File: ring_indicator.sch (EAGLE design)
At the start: 21 parts, among them Q2 BUZ11

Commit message: v0.2-produced
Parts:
- FRITZBOX, INPUT_12V, LICHT1, LICHT2, RUNDUMLEUCHTE: value (none) -> CON_23.81; device pinhead:PINHD-1X2 -> pcaroli:CON_23.81
- R1, R2, R3, R4: device rcl:R-EU_0204/5 -> rcl:R-EU_0207/10
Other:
- moved on the sheet: FRITZBOX, INPUT_12V, LICHT1, LICHT2, RUNDUMLEUCHTE
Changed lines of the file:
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@@
 <layer number="51" name="tDocu" color="6" fill="1" visible="no" active="no"/>
 <layer number="52" name="bDocu" color="7" fill="1" visible="no" active="no"/>
+<layer number="90" name="Modules" color="5" fill="1" visible="yes" active="yes"/>
 <layer number="91" name="Nets" color="2" fill="1" visible="yes" active="yes"/>
 <layer number="92" name="Busses" color="1" fill="1" visible="yes" active="yes"/>
@@
 <parts>
 <part name="PHONE_IN" library="con-wenzhou-yihua" deviceset="YH-55-10" device=""/>
-<part name="FRITZBOX" library="pinhead" deviceset="PINHD-1X2" device=""/>
-<part name="LICHT1" library="pinhead" deviceset="PINHD-1X2" device=""/>
-<part name="LICHT2" library="pinhead" deviceset="PINHD-1X2" device=""/>
-<part name="RUNDUMLEUCHTE" library="pinhead" deviceset="PINHD-1X2" device=""/>
+<part name="FRITZBOX" library="pcaroli" deviceset="CON_2" device="3.81"/>
+<part name="LICHT1" library="pcaroli" deviceset="CON_2" device="3.81"/>
+<part name="LICHT2" library="pcaroli" deviceset="CON_2" device="3.81"/>
+<part name="RUNDUMLEUCHTE" library="pcaroli" deviceset="CON_2" device="3.81"/>
 <part name="SUPPLY1" library="supply2" deviceset="GND" device=""/>
 <part name="P+1" library="supply1" deviceset="VCC" device=""/>
@@
 <part name="SUPPLY2" library="supply2" deviceset="GND" device=""/>
 <part name="SUPPLY3" library="supply2" deviceset="GND" device=""/>
-<part name="INPUT_12V" library="pinhead" deviceset="PINHD-1X2" device=""/>
+<part name="INPUT_12V" library="pcaroli" deviceset="CON_2" device="3.81"/>
 <part name="SUPPLY4" library="supply2" deviceset="GND" device=""/>
 <part name="P+4" library="supply1" deviceset="VCC" device=""/>
 <part name="C1" library="resistor" deviceset="C-EU" device="102-064X133" value="470n"/>
 <part name="C2" library="rcl" deviceset="CPOL-EU" device="E3.5-8" value="47u"/>
-<part name="R1" library="rcl" deviceset="R-EU_" device="0204/5" value="1M"/>
-<part name="R2" library="rcl" deviceset="R-EU_" device="0204/5" value="1k"/>
+<part name="R1" library="rcl" deviceset="R-EU_" device="0207/10" value="1M"/>
+<part name="R2" library="rcl" deviceset="R-EU_" device="0207/10" value="1k"/>
 <part name="D1" library="diode" deviceset="1N4004" device=""/>
 <part name="D2" library="diode" deviceset="1N4004" device=""/>
 <part name="D3" library="diode" deviceset="1N4004" device=""/>
 <part name="D4" library="diode" deviceset="1N4004" device=""/>
-<part name="R3" library="rcl" deviceset="R-EU_" device="0204/5" value="2k2"/>
+<part name="R3" library="rcl" deviceset="R-EU_" device="0207/10" value="2k2"/>
 <part name="LED1" library="led" deviceset="LED" device="5MM"/>
-<part name="R4" library="rcl" deviceset="R-EU_" device="0204/5" value="100k"/>
+<part name="R4" library="rcl" deviceset="R-EU_" device="0207/10" value="100k"/>
 <part name="OK1" library="optocoupler" deviceset="4N*?M" device="" technology="27"/>
 <part name="Q2" library="transistor-fet" deviceset="BUZ11" device=""/>
@@
 <instance part="LICHT1" gate="G$1" x="256.54" y="88.9" rot="MR180"/>
 <instance part="LICHT2" gate="G$1" x="256.54" y="60.96" rot="MR180"/>
-<instance part="RUNDUMLEUCHTE" gate="G$1" x="220.98" y="35.56" rot="MR180"/>
+<instance part="RUNDUMLEUCHTE" gate="G$1" x="220.98" y="33.02" rot="MR180"/>
 <instance part="SUPPLY1" gate="GND" x="246.38" y="109.22" rot="MR0"/>
 <instance part="P+1" gate="VCC" x="246.38" y="121.92" rot="MR0"/>
@@
 <segment>
 <pinref part="FRITZBOX" gate="G$1" pin="1"/>
-<wire x1="254" y1="114.3" x2="246.38" y2="114.3" width="0.1524" layer="91"/>
 <wire x1="246.38" y1="114.3" x2="246.38" y2="111.76" width="0.1524" layer="91"/>
 <pinref part="SUPPLY1" gate="GND" pin="GND"/>
@@
 <segment>
 <pinref part="LICHT1" gate="G$1" pin="1"/>
-<wire x1="254" y1="86.36" x2="246.38" y2="86.36" width="0.1524" layer="91"/>
 <wire x1="246.38" y1="86.36" x2="246.38" y2="83.82" width="0.1524" layer="91"/>
 <pinref part="SUPPLY2" gate="GND" pin="GND"/>
@@
 <segment>
 <pinref part="LICHT2" gate="G$1" pin="1"/>
-<wire x1="254" y1="58.42" x2="246.38" y2="58.42" width="0.1524" layer="91"/>
 <wire x1="246.38" y1="58.42" x2="246.38" y2="55.88" width="0.1524" layer="91"/>
 <pinref part="SUPPLY3" gate="GND" pin="GND"/>
@@
 <wire x1="68.58" y1="111.76" x2="68.58" y2="109.22" width="0.1524" layer="91"/>
 <pinref part="INPUT_12V" gate="G$1" pin="1"/>
-<wire x1="35.56" y1="116.84" x2="40.64" y2="116.84" width="0.1524" layer="91"/>
+<wire x1="43.18" y1="116.84" x2="40.64" y2="116.84" width="0.1524" layer="91"/>
 <wire x1="40.64" y1="116.84" x2="40.64" y2="111.76" width="0.1524" layer="91"/>
 <wire x1="40.64" y1="111.76" x2="50.8" y2="111.76" width="0.1524" layer="91"/>
@@
 <segment>
 <pinref part="FRITZBOX" gate="G$1" pin="2"/>
-<wire x1="254" y1="116.84" x2="246.38" y2="116.84" width="0.1524" layer="91"/>
 <wire x1="246.38" y1="116.84" x2="246.38" y2="119.38" width="0.1524" layer="91"/>
 <pinref part="P+1" gate="VCC" pin="VCC"/>
@@
 <segment>
 <pinref part="LICHT1" gate="G$1" pin="2"/>
-<wire x1="254" y1="88.9" x2="246.38" y2="88.9" width="0.1524" layer="91"/>
 <wire x1="246.38" y1="88.9" x2="246.38" y2="91.44" width="0.1524" layer="91"/>
 <pinref part="P+2" gate="VCC" pin="VCC"/>
@@
 <segment>
 <pinref part="LICHT2" gate="G$1" pin="2"/>
-<wire x1="254" y1="60.96" x2="246.38" y2="60.96" width="0.1524" layer="91"/>
 <wire x1="246.38" y1="60.96" x2="246.38" y2="63.5" width="0.1524" layer="91"/>
 <pinref part="P+3" gate="VCC" pin="VCC"/>
@@
 <pinref part="RUNDUMLEUCHTE" gate="G$1" pin="2"/>
 <pinref part="OK1" gate="G$1" pin="COL"/>
-<wire x1="187.96" y1="35.56" x2="218.44" y2="35.56" width="0.1524" layer="91"/>
+<wire x1="187.96" y1="35.56" x2="210.82" y2="35.56" width="0.1524" layer="91"/>
 <wire x1="182.88" y1="0" x2="187.96" y2="0" width="0.1524" layer="91"/>
 <wire x1="187.96" y1="0" x2="187.96" y2="35.56" width="0.1524" layer="91"/>
@@
 <wire x1="68.58" y1="124.46" x2="68.58" y2="127" width="0.1524" layer="91"/>
 <pinref part="INPUT_12V" gate="G$1" pin="2"/>
-<wire x1="35.56" y1="119.38" x2="40.64" y2="119.38" width="0.1524" layer="91"/>
+<wire x1="43.18" y1="121.92" x2="40.64" y2="119.38" width="0.1524" layer="91"/>
 <wire x1="40.64" y1="119.38" x2="40.64" y2="124.46" width="0.1524" layer="91"/>
 <wire x1="40.64" y1="124.46" x2="50.8" y2="124.46" width="0.1524" layer="91"/>
@@
 <segment>
 <pinref part="RUNDUMLEUCHTE" gate="G$1" pin="1"/>
-<wire x1="218.44" y1="33.02" x2="208.28" y2="33.02" width="0.1524" layer="91"/>
+<wire x1="210.82" y1="30.48" x2="208.28" y2="30.48" width="0.1524" layer="91"/>
 <pinref part="Q2" gate="G$1" pin="D"/>
-<wire x1="208.28" y1="0" x2="208.28" y2="33.02" width="0.1524" layer="91"/>
-</segment>
-</net>
+<wire x1="208.28" y1="0" x2="208.28" y2="30.48" width="0.1524" layer="91"/>
+</segment>
+</net>

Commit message: v0.2.1-cleanup
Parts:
- removed C3: (no value), capacitor-wima:C2,5-3
- removed C5: (no value), resistor:CPOL-EUTT2D6
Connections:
- net GND: no longer C3.2, C5.-
- net VCC: no longer C3.1, C5.+
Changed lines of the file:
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@@
 <part name="SUPPLY6" library="supply2" deviceset="GND" device=""/>
 <part name="SUPPLY7" library="supply2" deviceset="GND" device=""/>
-<part name="C3" library="capacitor-wima" deviceset="C" device="2,5-3"/>
-<part name="C5" library="resistor" deviceset="CPOL-EU" device="TT2D6"/>
 </parts>
 <sheets>
@@
 <instance part="SUPPLY3" gate="GND" x="246.38" y="53.34" rot="MR0"/>
 <instance part="INPUT_12V" gate="G$1" x="33.02" y="119.38" rot="R180"/>
-<instance part="SUPPLY4" gate="GND" x="68.58" y="106.68"/>
-<instance part="P+4" gate="VCC" x="68.58" y="129.54"/>
+<instance part="SUPPLY4" gate="GND" x="43.18" y="111.76"/>
+<instance part="P+4" gate="VCC" x="43.18" y="127"/>
 <instance part="C1" gate="G$1" x="93.98" y="15.24" rot="R270"/>
 <instance part="C2" gate="G$1" x="185.42" y="-17.78"/>
@@
 <instance part="SUPPLY6" gate="GND" x="185.42" y="-25.4"/>
 <instance part="SUPPLY7" gate="GND" x="210.82" y="-25.4"/>
-<instance part="C3" gate="G$1" x="50.8" y="119.38"/>
-<instance part="C5" gate="G$1" x="58.42" y="119.38"/>
 </instances>
 <busses>
@@
 </segment>
 <segment>
+<pinref part="INPUT_12V" gate="G$1" pin="1"/>
 <pinref part="SUPPLY4" gate="GND" pin="GND"/>
-<wire x1="68.58" y1="111.76" x2="68.58" y2="109.22" width="0.1524" layer="91"/>
-<pinref part="INPUT_12V" gate="G$1" pin="1"/>
-<wire x1="43.18" y1="116.84" x2="40.64" y2="116.84" width="0.1524" layer="91"/>
-<wire x1="40.64" y1="116.84" x2="40.64" y2="111.76" width="0.1524" layer="91"/>
-<wire x1="40.64" y1="111.76" x2="50.8" y2="111.76" width="0.1524" layer="91"/>
-<wire x1="50.8" y1="111.76" x2="58.42" y2="111.76" width="0.1524" layer="91"/>
-<wire x1="58.42" y1="111.76" x2="68.58" y2="111.76" width="0.1524" layer="91"/>
-<wire x1="58.42" y1="111.76" x2="58.42" y2="114.3" width="0.1524" layer="91"/>
-<junction x="58.42" y="111.76"/>
-<pinref part="C3" gate="G$1" pin="2"/>
-<wire x1="50.8" y1="111.76" x2="50.8" y2="114.3" width="0.1524" layer="91"/>
-<junction x="50.8" y="111.76"/>
-<pinref part="C5" gate="G$1" pin="-"/>
+<wire x1="43.18" y1="116.84" x2="43.18" y2="114.3" width="0.1524" layer="91"/>
 </segment>
 </net>
@@
 </segment>
 <segment>
+<pinref part="INPUT_12V" gate="G$1" pin="2"/>
+<wire x1="43.18" y1="121.92" x2="43.18" y2="124.46" width="0.1524" layer="91"/>
 <pinref part="P+4" gate="VCC" pin="VCC"/>
-<wire x1="68.58" y1="124.46" x2="68.58" y2="127" width="0.1524" layer="91"/>
-<pinref part="INPUT_12V" gate="G$1" pin="2"/>
-<wire x1="43.18" y1="121.92" x2="40.64" y2="119.38" width="0.1524" layer="91"/>
-<wire x1="40.64" y1="119.38" x2="40.64" y2="124.46" width="0.1524" layer="91"/>
-<wire x1="40.64" y1="124.46" x2="50.8" y2="124.46" width="0.1524" layer="91"/>
-<wire x1="50.8" y1="124.46" x2="58.42" y2="124.46" width="0.1524" layer="91"/>
-<wire x1="58.42" y1="124.46" x2="68.58" y2="124.46" width="0.1524" layer="91"/>
-<wire x1="58.42" y1="124.46" x2="58.42" y2="121.92" width="0.1524" layer="91"/>
-<junction x="58.42" y="124.46"/>
-<pinref part="C3" gate="G$1" pin="1"/>
-<wire x1="50.8" y1="124.46" x2="50.8" y2="121.92" width="0.1524" layer="91"/>
-<junction x="50.8" y="124.46"/>
-<pinref part="C5" gate="G$1" pin="+"/>
 </segment>
 </net>

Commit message: v0.2.2-layout simplified
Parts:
- R4: value 100k -> 50k
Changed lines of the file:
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@@
 <part name="R3" library="rcl" deviceset="R-EU_" device="0207/10" value="2k2"/>
 <part name="LED1" library="led" deviceset="LED" device="5MM"/>
-<part name="R4" library="rcl" deviceset="R-EU_" device="0207/10" value="100k"/>
+<part name="R4" library="rcl" deviceset="R-EU_" device="0207/10" value="50k"/>
 <part name="OK1" library="optocoupler" deviceset="4N*?M" device="" technology="27"/>
 <part name="Q2" library="transistor-fet" deviceset="BUZ11" device=""/>
@@
 <instance part="RUNDUMLEUCHTE" gate="G$1" x="220.98" y="33.02" rot="MR180"/>
 <instance part="SUPPLY1" gate="GND" x="246.38" y="109.22" rot="MR0"/>
-<instance part="P+1" gate="VCC" x="246.38" y="121.92" rot="MR0"/>
-<instance part="P+2" gate="VCC" x="246.38" y="93.98" rot="MR0"/>
-<instance part="P+3" gate="VCC" x="246.38" y="66.04" rot="MR0"/>
+<instance part="P+1" gate="VCC" x="246.38" y="124.46" rot="MR0"/>
+<instance part="P+2" gate="VCC" x="246.38" y="96.52" rot="MR0"/>
+<instance part="P+3" gate="VCC" x="246.38" y="68.58" rot="MR0"/>
 <instance part="SUPPLY2" gate="GND" x="246.38" y="81.28" rot="MR0"/>
 <instance part="SUPPLY3" gate="GND" x="246.38" y="53.34" rot="MR0"/>
@@
 <segment>
 <pinref part="FRITZBOX" gate="G$1" pin="2"/>
-<wire x1="246.38" y1="116.84" x2="246.38" y2="119.38" width="0.1524" layer="91"/>
 <pinref part="P+1" gate="VCC" pin="VCC"/>
+<wire x1="246.38" y1="121.92" x2="246.38" y2="119.38" width="0.1524" layer="91"/>
 </segment>
 <segment>
 <pinref part="LICHT1" gate="G$1" pin="2"/>
-<wire x1="246.38" y1="88.9" x2="246.38" y2="91.44" width="0.1524" layer="91"/>
 <pinref part="P+2" gate="VCC" pin="VCC"/>
+<wire x1="246.38" y1="93.98" x2="246.38" y2="91.44" width="0.1524" layer="91"/>
 </segment>
 <segment>
 <pinref part="LICHT2" gate="G$1" pin="2"/>
-<wire x1="246.38" y1="60.96" x2="246.38" y2="63.5" width="0.1524" layer="91"/>
 <pinref part="P+3" gate="VCC" pin="VCC"/>
+<wire x1="246.38" y1="66.04" x2="246.38" y2="63.5" width="0.1524" layer="91"/>
 </segment>
 <segment>

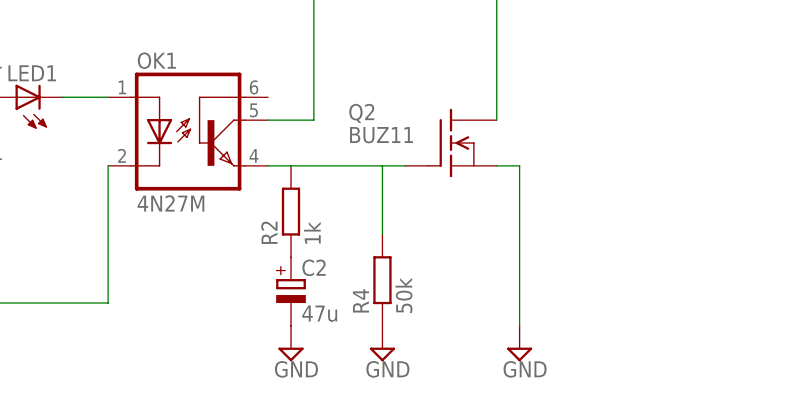
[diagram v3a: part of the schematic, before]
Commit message: light timing changed
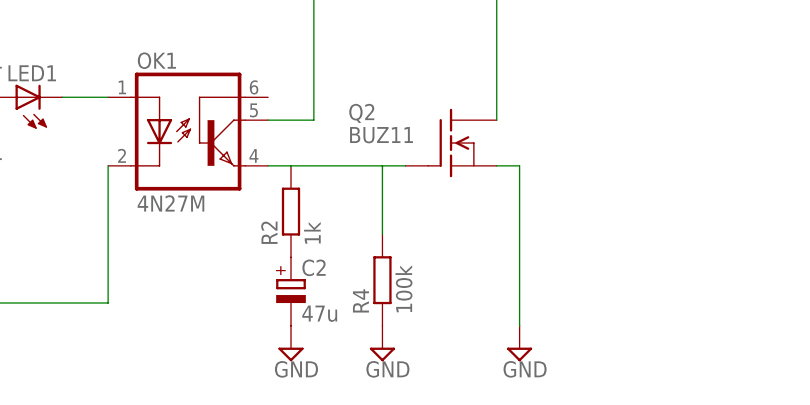
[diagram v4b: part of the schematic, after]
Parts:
- R4: value 50k -> 100k
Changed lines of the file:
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@@
 <part name="R3" library="rcl" deviceset="R-EU_" device="0207/10" value="2k2"/>
 <part name="LED1" library="led" deviceset="LED" device="5MM"/>
-<part name="R4" library="rcl" deviceset="R-EU_" device="0207/10" value="50k"/>
+<part name="R4" library="rcl" deviceset="R-EU_" device="0207/10" value="100k"/>
 <part name="OK1" library="optocoupler" deviceset="4N*?M" device="" technology="27"/>
 <part name="Q2" library="transistor-fet" deviceset="BUZ11" device=""/>

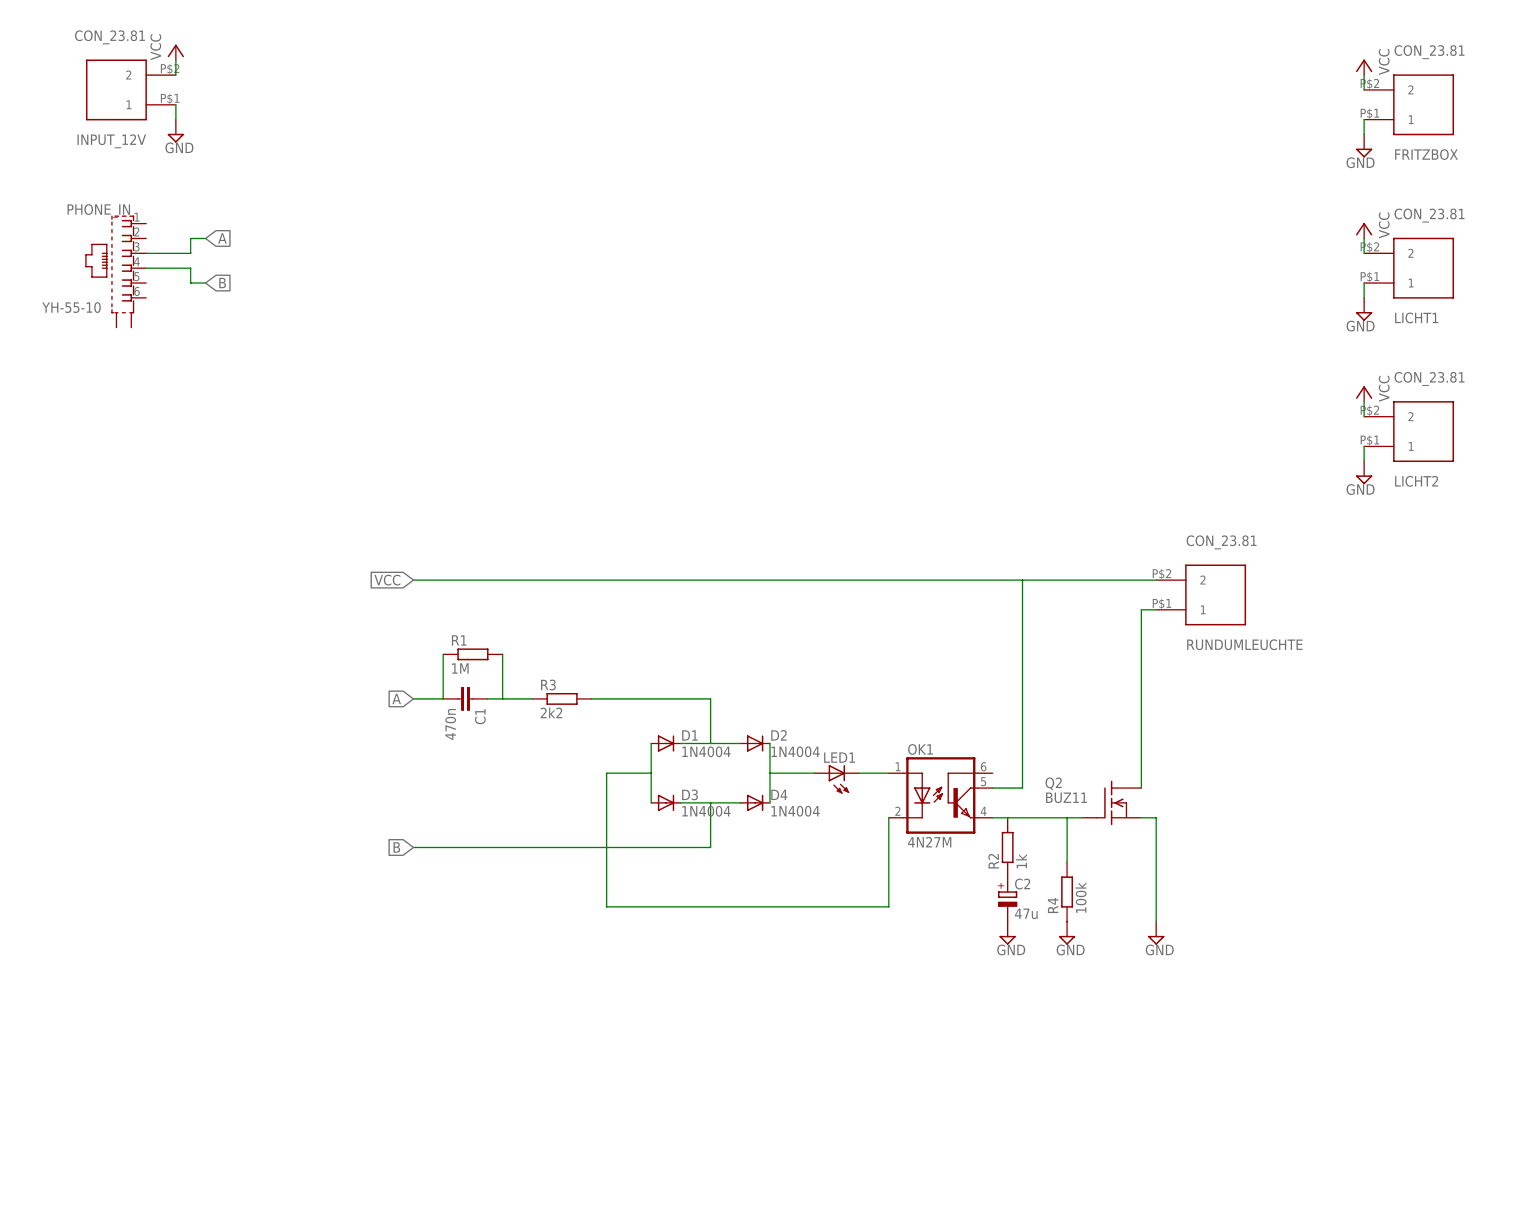
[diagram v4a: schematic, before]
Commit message: basic poe injector added
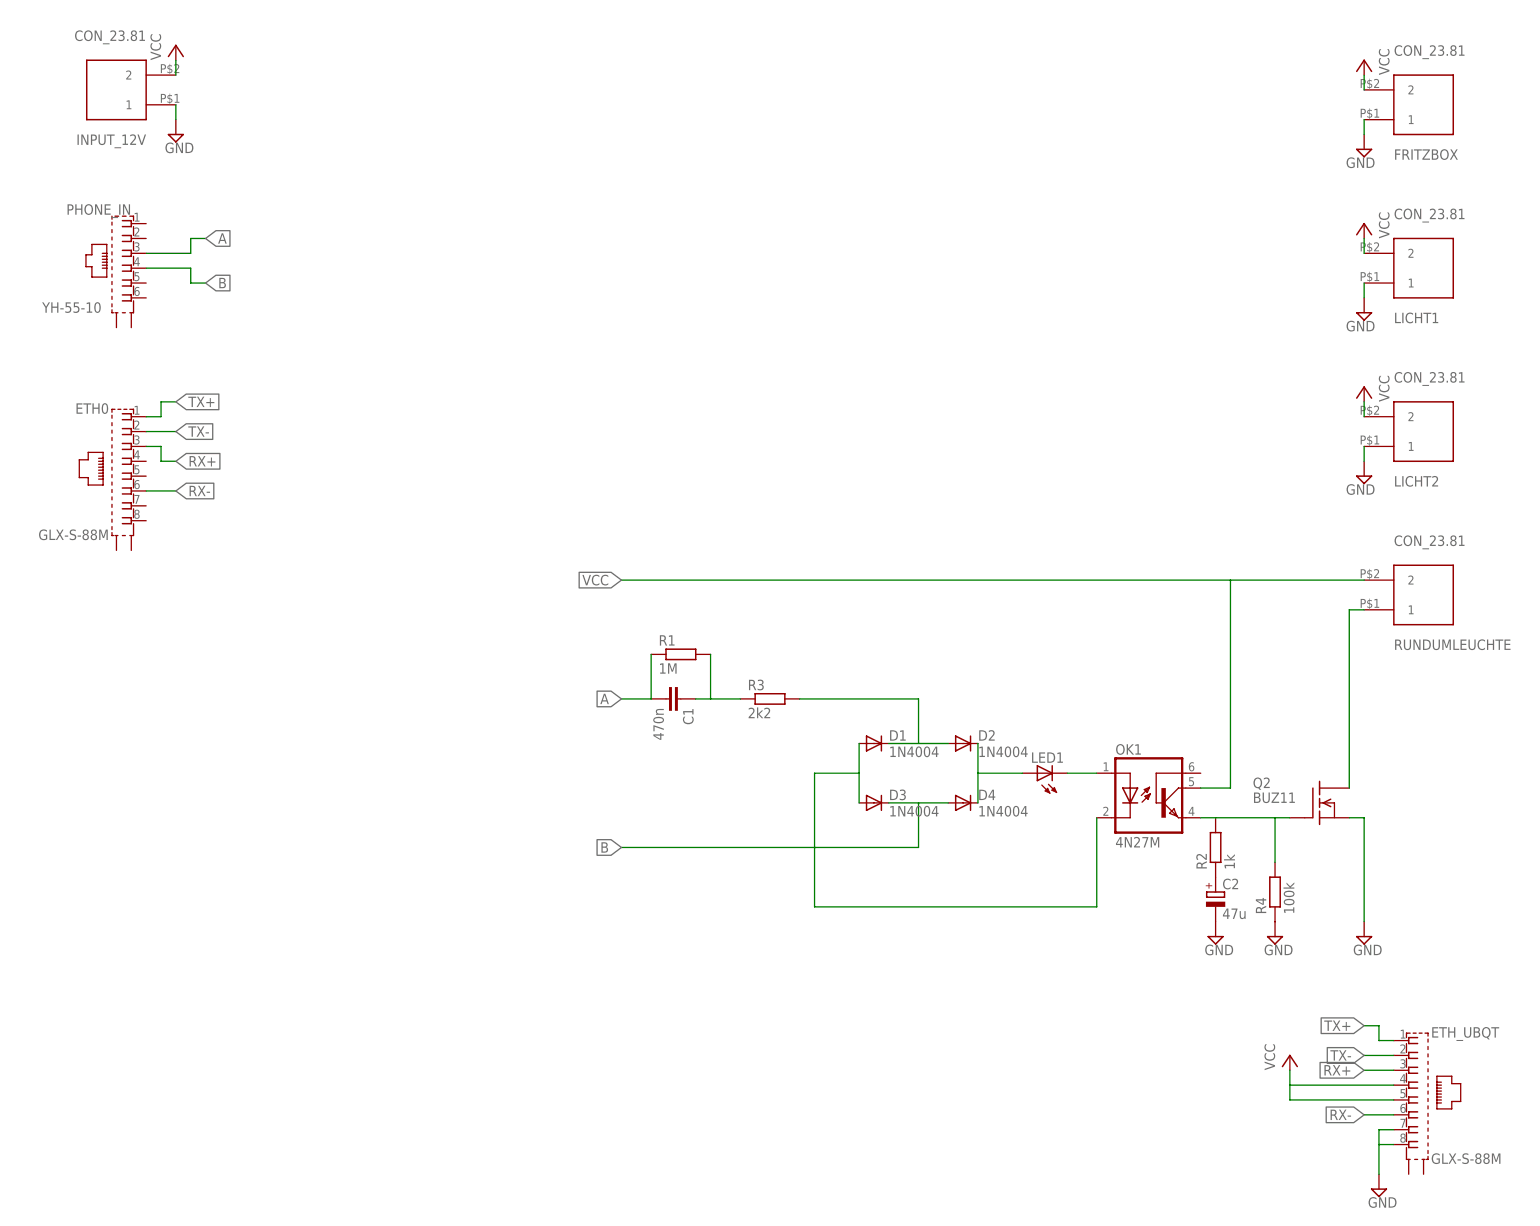
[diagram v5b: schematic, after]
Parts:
- added ETH0, ETH_UBQT: GLX-S-88M, con-kycon:GLX-S-88M
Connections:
- new net RX+: ETH0.3, ETH_UBQT.3
- new net RX-: ETH0.6, ETH_UBQT.6
- new net TX+: ETH0.1, ETH_UBQT.1
- new net TX-: ETH0.2, ETH_UBQT.2
- net GND: now also ETH_UBQT.7, ETH_UBQT.8
- net VCC: now also ETH_UBQT.4, ETH_UBQT.5
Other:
- moved on the sheet: C1, C2, D1, D2, D3, D4, LED1, OK1, Q2, R1, R2, R3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
